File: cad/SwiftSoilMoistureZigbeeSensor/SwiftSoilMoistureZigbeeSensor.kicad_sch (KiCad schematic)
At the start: 13 parts, among them J1 Probe, J2 BAT, J3 ARM SWD, Q1 BSS84, SW1 Factory Reset, U1 TPS61221DCK, U2 E73-2G4M08S1C

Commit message: PCB Version 1.1
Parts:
- removed J2: BAT, Connector_PinHeader_2.54mm:PinHeader_1x02_P2.54mm_Vertical, symbol Connector:Conn_01x02_Pin
- added BT1: CR2032, Battery:BatteryHolder_Keystone_1060_1x2032, symbol Device:Battery_Cell
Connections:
- net GND: now also BT1.2 (-)
- net at C1.1, L1.1, U1.1 (VIN)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: now also BT1.1 (+)
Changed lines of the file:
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@@
-    (stroke (width 0) (type default))
-  )
-  (wire (pts (xy 162.56 54.61) (xy 162.56 60.96))
     (stroke (width 0) (type default))
   )
@@
     (stroke (width 0) (type default))
   )
-  (wire (pts (xy 162.56 52.07) (xy 171.45 52.07))
+  (wire (pts (xy 156.21 52.07) (xy 171.45 52.07))
     (stroke (width 0) (type default))
   )
@@
     (stroke (width 0) (type default))
   )
-  (wire (pts (xy 162.56 60.96) (xy 171.45 60.96))
+  (wire (pts (xy 156.21 60.96) (xy 171.45 60.96))
+    (stroke (width 0) (type default))
+  )
+  (wire (pts (xy 156.21 60.96) (xy 156.21 59.69))
     (stroke (width 0) (type default))
   )
@@
         (path "/abcc6947-5804-4900-9240-6fa6b27c7542"
           (reference "L1") (unit 1)
-        )
-      )
-    )
-  )
-  (symbol (lib_id "Connector:Conn_01x02_Pin") (at 157.48 52.07 0) (unit 1)
-    (in_bom yes) (on_board yes) (dnp no) (fields_autoplaced)
-    (property "Reference" "J2" (at 158.115 46.99 0)
-      (effects (font (size 1.27 1.27)))
-    )
-    (property "Value" "BAT" (at 158.115 49.53 0)
-      (effects (font (size 1.27 1.27)))
-    )
-    (property "Footprint" "Connector_PinHeader_2.54mm:PinHeader_1x02_P2.54mm_Vertical" (at 157.48 52.07 0)
-      (effects (font (size 1.27 1.27)) hide)
-    )
-    (property "Datasheet" "~" (at 157.48 52.07 0)
-      (effects (font (size 1.27 1.27)) hide)
-    )
-    (property "LCSC" "C180247" (at 157.48 52.07 0)
-      (effects (font (size 1.27 1.27)) hide)
-    )
-    (pin "1")
-    (pin "2")
-    (instances
-      (project "SwiftSoilMoistureZigbeeSensor"
-        (path "/abcc6947-5804-4900-9240-6fa6b27c7542"
-          (reference "J2") (unit 1)
         )
       )
@@
         )
       )
+    )
+  )
+  (symbol (lib_id "Device:Battery_Cell") (at 156.21 57.15 0) (unit 1)
+    (in_bom yes) (on_board yes) (dnp no)
+    (property "Reference" "BT1" (at 148.59 54.61 0)
+      (effects (font (size 1.27 1.27)) (justify left))
+    )
+    (property "Value" "CR2032" (at 147.32 58.42 0)
+      (effects (font (size 1.27 1.27)) (justify left))
+    )
+    (property "Footprint" "Battery:BatteryHolder_Keystone_1060_1x2032" (at 156.21 55.626 90)
+      (effects (font (size 1.27 1.27)) hide)
+    )
+    (property "Datasheet" "~" (at 156.21 55.626 90)
+      (effects (font (size 1.27 1.27)) hide)
+    )
+    (pin "2")
+    (pin "1")
+    (instances
+      (project "SwiftSoilMoistureZigbeeSensor"
+        (path "/abcc6947-5804-4900-9240-6fa6b27c7542"
+          (reference "BT1") (unit 1)
+        )
+      )

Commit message: Updated LCSC BOM
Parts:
- BT1: LCSC (none) -> C22363833
- J1: LCSC C7089182 -> Male C2935928 / Female C7089182
- J3: LCSC (none) -> C49257
- JP1: LCSC C180247 + C3715628 -> C492401 + C3715628
- L1: LCSC C87172 -> C87172
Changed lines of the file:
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@@
       (effects (font (size 1.27 1.27)) hide)
     )
-    (property "LCSC" " C7089182" (at 246.38 88.9 0)
+    (property "LCSC" "Male C2935928 / Female C7089182" (at 246.38 88.9 0)
       (effects (font (size 1.27 1.27)) hide)
     )
@@
       (effects (font (size 1.27 1.27)) hide)
     )
-    (property "LCSC" " C87172" (at 175.26 49.53 0)
+    (property "LCSC" "C87172" (at 175.26 49.53 0)
       (effects (font (size 1.27 1.27)) hide)
     )
@@
       (effects (font (size 1.27 1.27)) hide)
     )
-    (property "LCSC" "C180247 + C3715628" (at 227.33 40.64 0)
+    (property "LCSC" "C492401 + C3715628" (at 227.33 40.64 0)
       (effects (font (size 1.27 1.27)) hide)
     )
@@
       (effects (font (size 1.27 1.27)) hide)
     )
-    (property "LCSC" "" (at 46.99 102.87 0)
+    (property "LCSC" "C49257" (at 46.99 102.87 0)
       (effects (font (size 1.27 1.27)) hide)
     )
@@
       (effects (font (size 1.27 1.27)) hide)
     )
+    (property "LCSC" "C22363833" (at 156.21 57.15 0)
+      (effects (font (size 1.27 1.27)) hide)
+    )

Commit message: Change LCSC part ref
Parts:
- J3: LCSC C49257 -> C6332197
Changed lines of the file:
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@@
       (effects (font (size 1.27 1.27)) hide)
     )
-    (property "LCSC" "C49257" (at 46.99 102.87 0)
+    (property "LCSC" "C6332197" (at 46.99 102.87 0)
       (effects (font (size 1.27 1.27)) hide)
     )

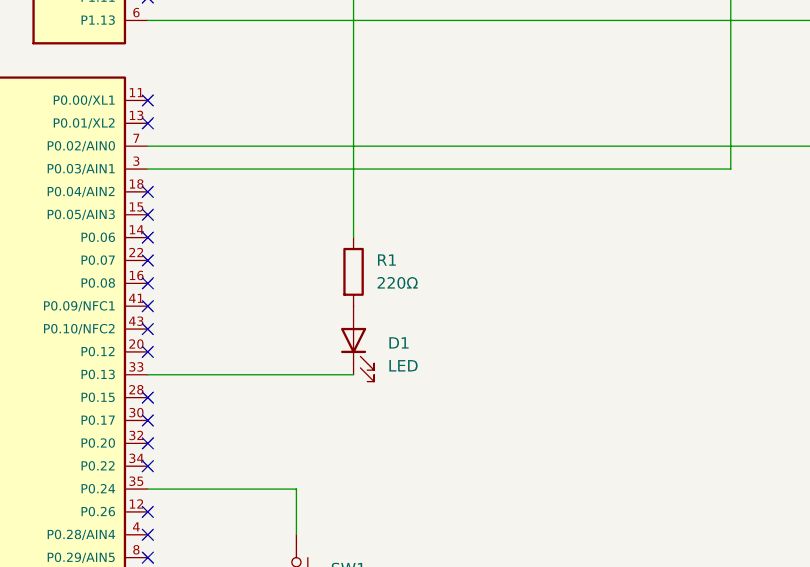
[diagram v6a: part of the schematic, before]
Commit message: 680ohm is enough. SWD silk text for convinience
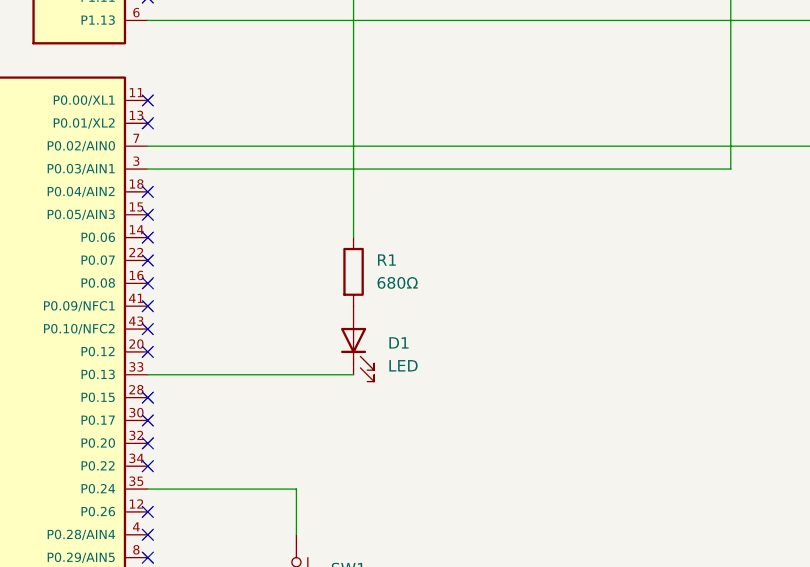
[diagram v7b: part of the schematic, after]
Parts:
- R1: value 220Ω -> 680Ω
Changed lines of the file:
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@@
       (effects (font (size 1.27 1.27)) (justify left))
     )
-    (property "Value" "220Ω" (at 139.7 101.6 0)
+    (property "Value" "680Ω" (at 139.7 101.6 0)
       (effects (font (size 1.27 1.27)) (justify left))
     )

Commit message: Inductance footprint modified. Probe print
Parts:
- L1: footprint Inductor_SMD:L_Wuerth_MAPI-4020 -> Inductor_SMD:L_Taiyo-Yuden_NR-30xx
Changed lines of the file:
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@@
       (effects (font (size 1.27 1.27)))
     )
-    (property "Footprint" "Inductor_SMD:L_Wuerth_MAPI-4020" (at 175.26 49.53 0)
+    (property "Footprint" "Inductor_SMD:L_Taiyo-Yuden_NR-30xx" (at 175.26 49.53 0)
       (effects (font (size 1.27 1.27)) hide)
     )
